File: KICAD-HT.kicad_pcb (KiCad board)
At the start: 2 copper layers, 90 x 70 mm, 86 parts, among them J1 HV80_IN, Q1 IPD050N10N5, Q2 IPD050N10N5, Q3 BSS127I, Q4 MMBT2222, Q5 BSS127I, T1 MSD1514-103ME, U1 UCC27517, U10 ISO7710, U11 AMC0311R, U12 UCC24612, U3 ISO7710, U5 DPC817, U7 AMC0311R, U8 AMC0311R, U9 AMC0302R

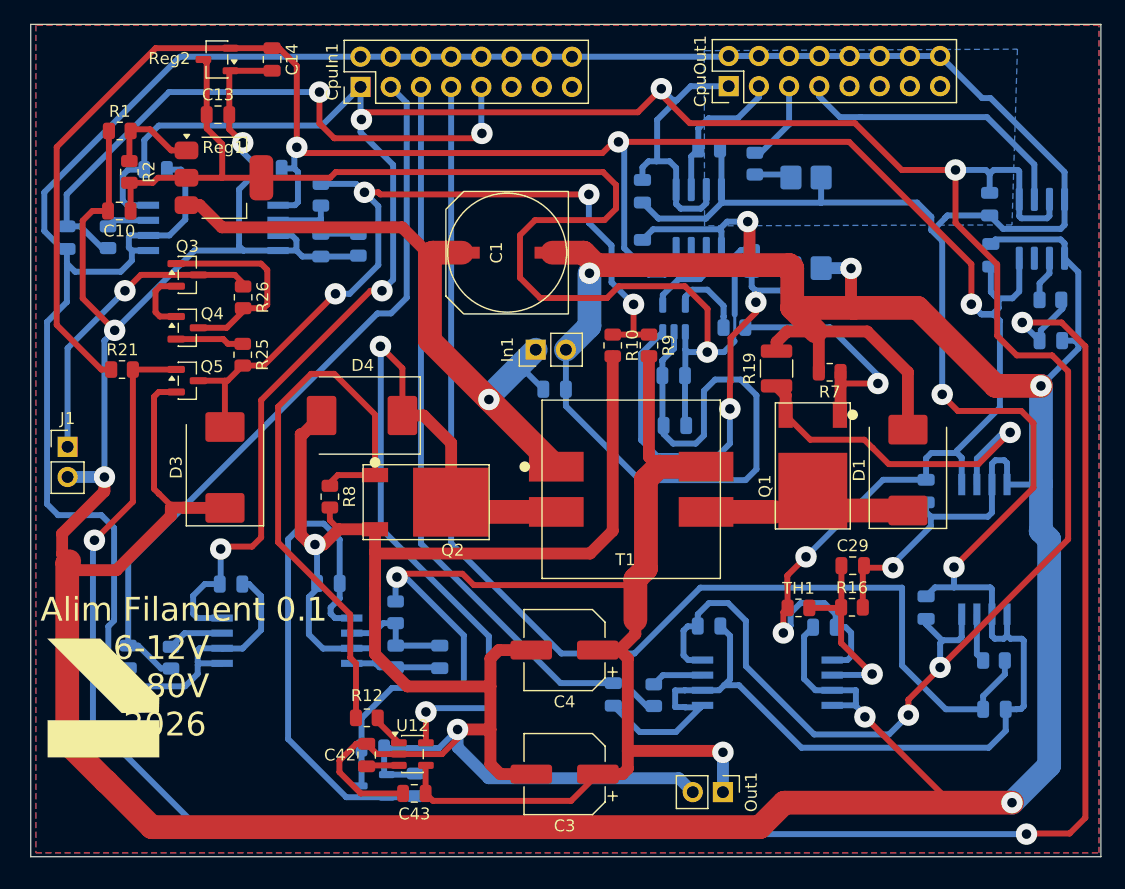
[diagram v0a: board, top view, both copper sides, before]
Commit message: Finalise le renommage alim-flyback-filament -> KICAD-HT et partage TO252
- Renommage du depot (fichiers deja renommes localement, jamais commite) :
  KICAD-HT.kicad_pcb/.kicad_pro/.kicad_sch, doc/KICAD-HT.png, references
  mises a jour (README.md, gen_composants.py PROJECT=, 00-intention-
  conception.md, doc/sim-vs-mesure.md, simulation/gen_asc.py).
  alim/isolation/polarisation.kicad_sch : resauvegarde native KiCad
  (reformatage), pas de changement electrique.
- bom_family_report.py : plus de chemin KiCad code en dur, detection
  dynamique du titre de projet (deja fait en session precedente, jamais
  commite).
- TO252 bascule vers la bibliotheque partagee lib_fp_commun/ (voir
  KICAD.md) : fp-lib-table pointe maintenant vers
  ${KIPRJMOD}/../lib_fp_commun/TO252.pretty au lieu de la copie locale,
  copie locale supprimee. Autres empreintes custom (A786, MSD1514,
  SOIC_DWV) : chemin de modele 3D repointe vers lib_fp_commun/ (les
  fichiers sources ont ete deplaces hors de composants-datasheets/datasheets/,
  qui ne garde plus que des PDF).

Co-Authored-By: Claude Sonnet 5 <noreply@anthropic.com>
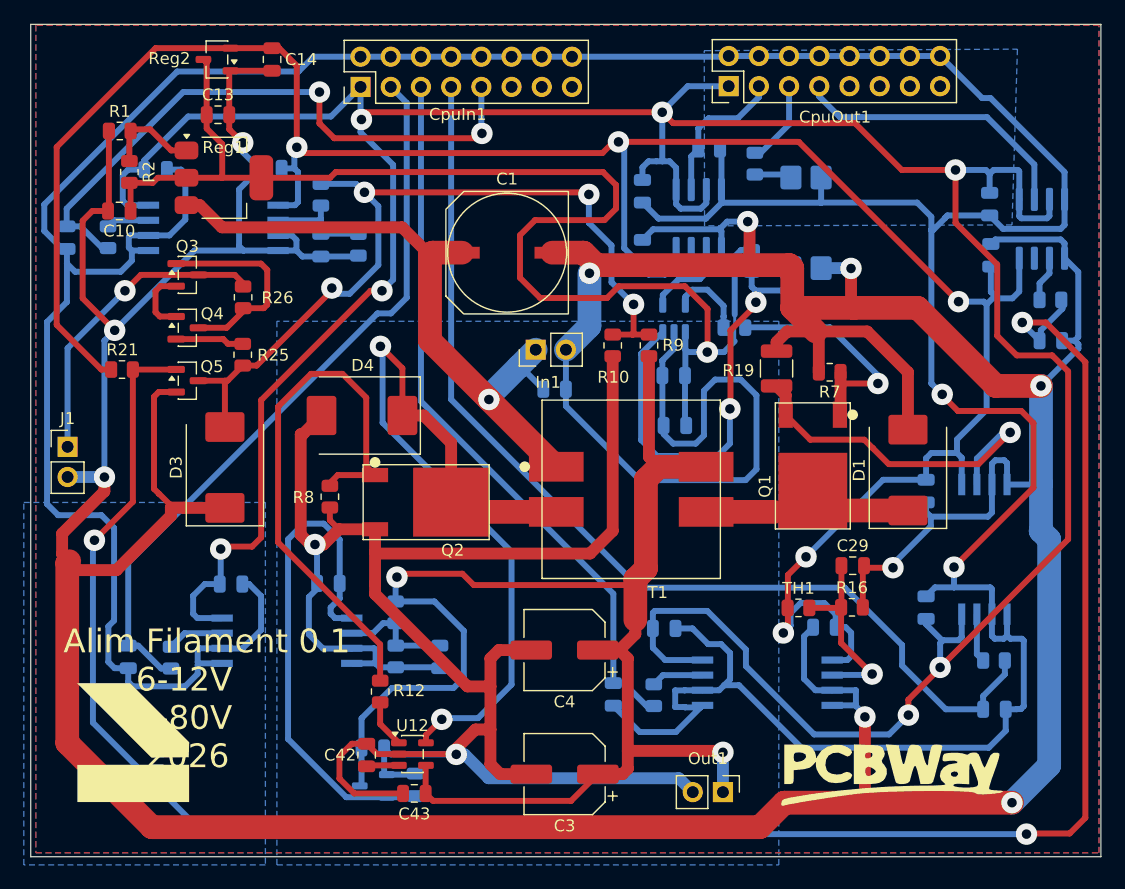
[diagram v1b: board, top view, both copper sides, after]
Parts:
- added G***: LOGO, lebel:pcbway-logo-small, F.Cu at (98.7, 83.6)
- moved ? 4.51 mm to (34.9, 81.2)
- moved C26 3.78 mm to (79.3, 71.6)
- moved R12 2.48 mm to (55.4, 76.9), turned to 90 degrees
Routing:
- net ISENSE_PRI_FBACK: track 102.2 -> 87.7 mm
- net RAIL_3V3_PRI: track 207.1 -> 202.5 mm
- net VOUT_N: track 172.2 -> 167.7 mm
- net GND: track 482.0 -> 486.3 mm
- net TEMP_PRI_FBACK: track 63.6 -> 61.0 mm
- net GND_CTRL: track 348.6 -> 350.8 mm
- net GATE_Q2: track 49.0 -> 47.1 mm
- net 3V3_CTRL: track 277.4 -> 275.8 mm
- net Net-(U12-VG): track 2.84 -> 4.05 mm
- net VOUT_P: track 125.3 -> 124.2 mm
- net SW_SEC: track 68.1 -> 69.0 mm
- net VAR_GATE: track 175.6 -> 174.8 mm
- net BIAS_FBACK: track 53.1 -> 52.4 mm
- net HV_BIAS: track 69.8 -> 70.3 mm
- added copper zone on B.Cu, net VOUT_N

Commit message: Bascule les empreintes custom (MSD1514, A786, SOIC_DWV) et logos (lebel/pcbway) vers lib_fp_commun
Supprime les copies locales redondantes, ajoute Symbol_commun/Graphic
(bibliotheques standard KiCad partagees) au fp-lib-table. Les logos
places sur le PCB passent du nickname lebel/lib au nickname partage
artwork (lib_id renomme directement sur les instances, pas de symbole
schema pour ces footprints decoratifs).

Co-Authored-By: Claude Sonnet 5 <noreply@anthropic.com>
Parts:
- removed ?: LOGO, lebel:lebel-logo
- removed CpuIn1: CTRL_C2000_IN, Connector_PinHeader_2.54mm:PinHeader_2x08_P2.54mm_Vertical
- removed CpuOut1: CTRL_C2000_OUT, Connector_PinHeader_2.54mm:PinHeader_2x08_P2.54mm_Vertical
- added G***: LOGO, artwork:lebel-logo-cartouche, F.Cu at (34.3, 82.3)
- added J2: NAPPE_FILAMENT_HT, Connector_IDC:IDC-Header_2x10_P2.54mm_Vertical, F.Cu at (127.4, 33.3)
- G***: footprint lebel:pcbway-logo-small -> artwork:pcbway-logo-small
- moved G*** 47.1 mm to (99.6, 36.6)
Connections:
- net 3V3_CTRL renamed 3V3_ISO
- net BIAS_FBACK renamed V_bias
- net ISENSE_PRI_FBACK renamed I_Shunt_ht
- net PWM_PRI_IN renamed PWM_ht
- net TEMP_PRI_FBACK renamed Temp_ht
- net VOUT_FBACK renamed Vht
- R3 pad 1: EN_PRI_IN -> PWM_EN
- U10 pad 2: PWM_BIAS_IN -> PWM_bias
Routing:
- net PWM_bias: track 0.00 -> 24.3 mm
- net PWM_BIAS_IN: track 24.3 -> 0.00 mm
- net PWM_EN: track 0.00 -> 7.10 mm
- net EN_PRI_IN: track 7.10 -> 0.00 mm

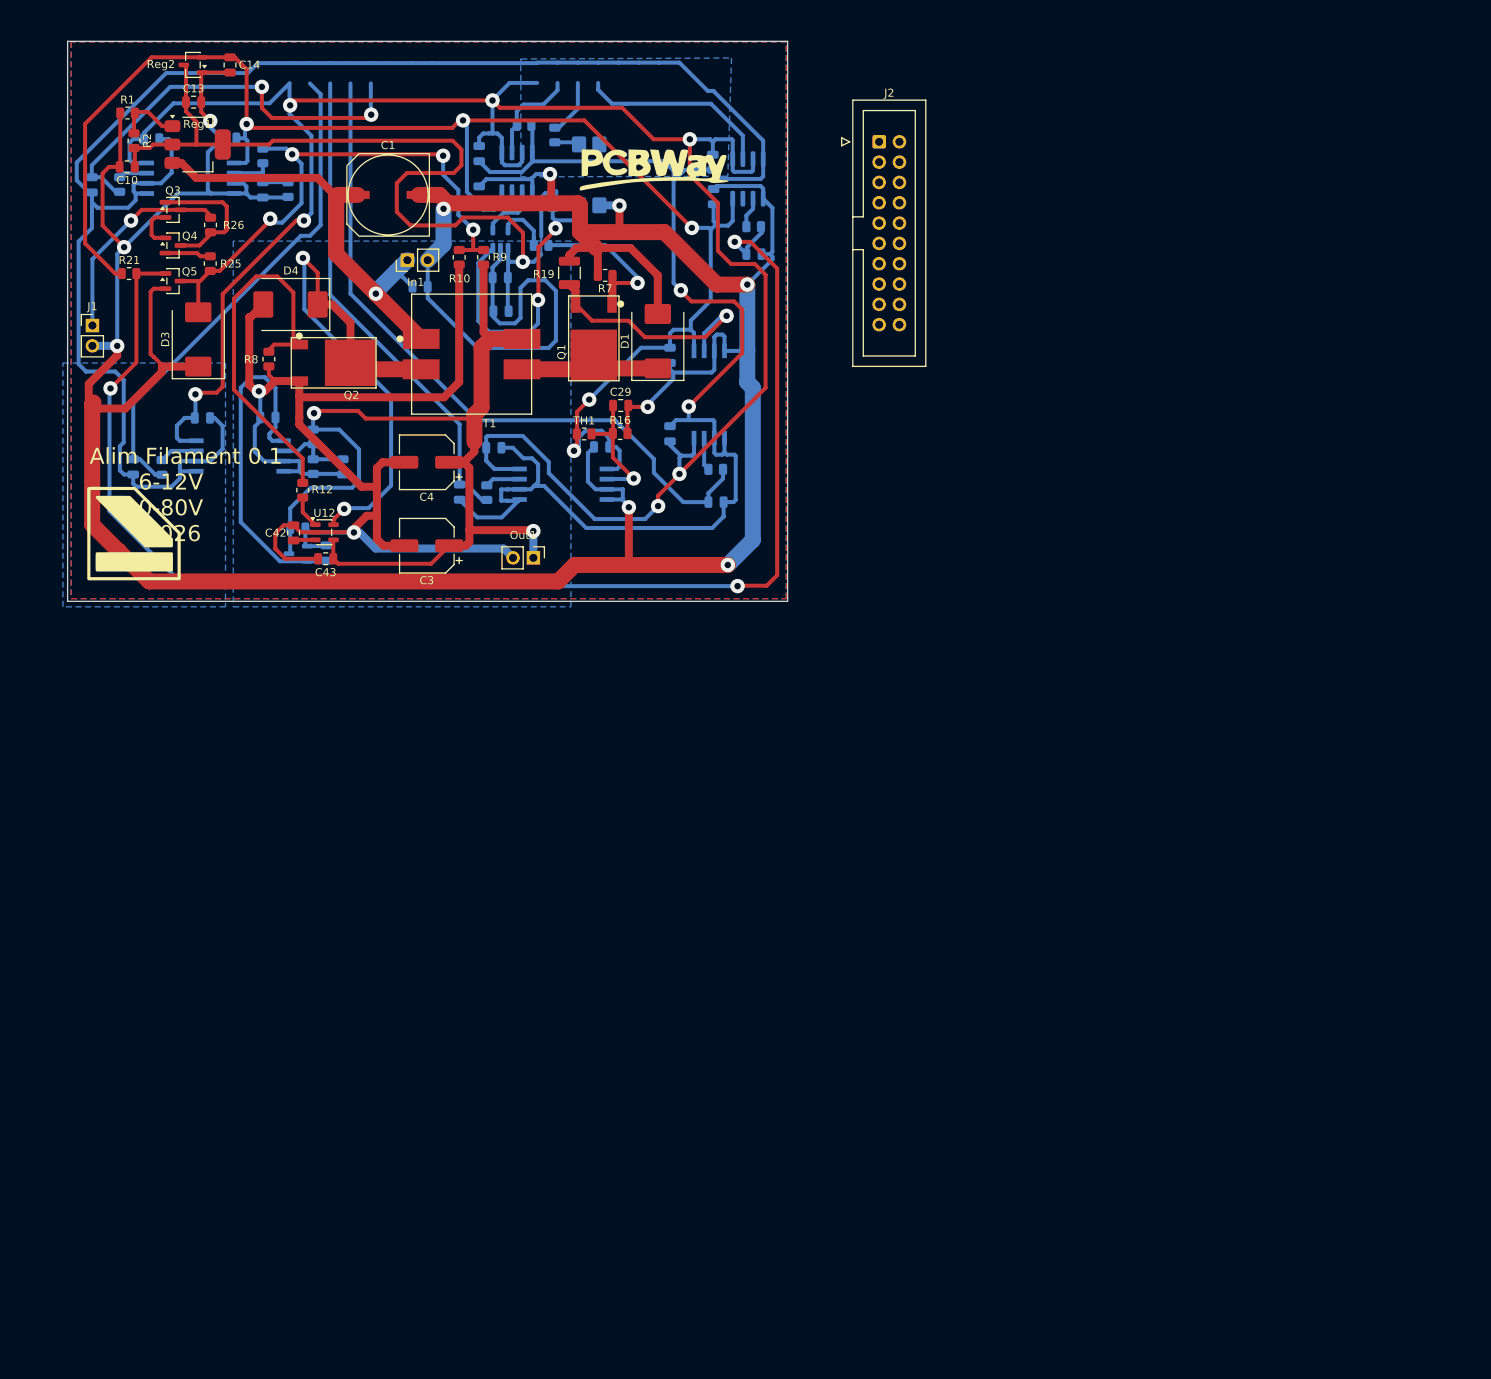
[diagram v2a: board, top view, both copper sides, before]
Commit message: Ajoute une LED de defaut sur Q_TRIP (R34/D6), corrige un bug d'insertion lib_symbols
Q_TRIP (sortie de reserve du verrou) recoit un usage reel : LED rouge 3mm
+ 10k, polarite ajustee par l'utilisateur pour s'allumer en defaut latche
(Q_TRIP -> D6 -> R34 -> GND, verifie par export netlist).

Corrige au passage une insertion incorrecte du bloc lib_symbols de
Device:LED (imbrique par erreur dans l'etiquette globale ISNS_AMP au lieu
de suivre la vraie fermeture de lib_symbols), qui empechait le chargement
de la feuille. Documente dans l'addendum du S19.

Co-Authored-By: Claude Sonnet 5 <noreply@anthropic.com>
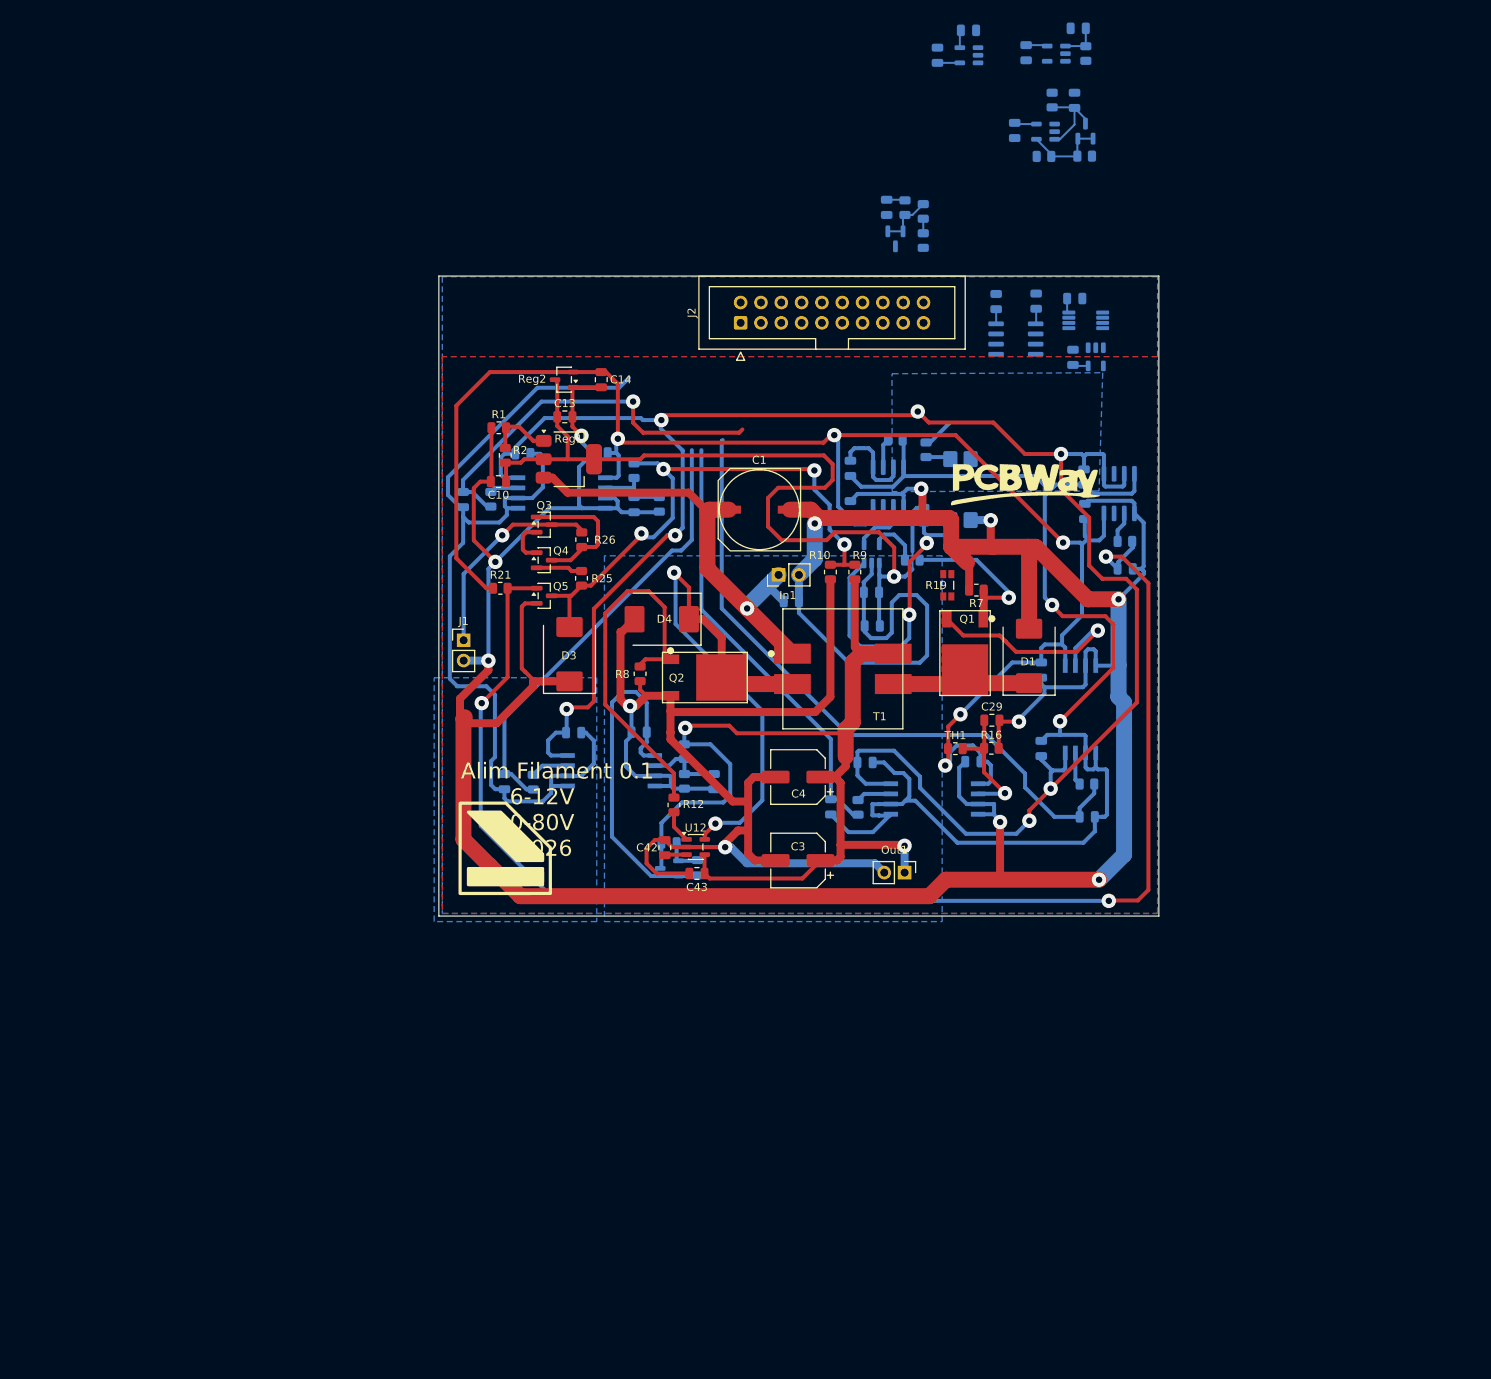
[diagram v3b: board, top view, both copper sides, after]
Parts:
- added C46: 100n, Capacitor_SMD:C_0805_2012Metric, B.Cu at (151.7, 60.2)
- added C47: 22p, Capacitor_SMD:C_0805_2012Metric, B.Cu at (151.8, 28.1)
- added C48: 100n, Capacitor_SMD:C_0805_2012Metric, B.Cu at (144.4, 31.9)
- added C50: 1n, Capacitor_SMD:C_0805_2012Metric, B.Cu at (134.7, 22.5)
- added C51: 100n, Capacitor_SMD:C_0805_2012Metric, B.Cu at (145.8, 22.2)
- added C52: 100p, Capacitor_SMD:C_0805_2012Metric, B.Cu at (152.3, 19.1)
- added C53: 100n, Capacitor_SMD:C_0805_2012Metric, B.Cu at (151.9, 52.9)
- added C54: 100n, Capacitor_SMD:C_0805_2012Metric, B.Cu at (138.6, 19.4)
- added C55: 100n, Capacitor_SMD:C_0805_2012Metric, B.Cu at (128.4, 41.5)
- added C56: 100n, Capacitor_SMD:C_0805_2012Metric, B.Cu at (142.1, 53.3)
- added C57: 100n, Capacitor_SMD:C_0805_2012Metric, B.Cu at (147.1, 53.2)
- added D5: BAT54S, Package_TO_SOT_SMD:SOT-23, B.Cu at (153.2, 32.0)
- added R27: 1k, Resistor_SMD:R_0805_2012Metric, B.Cu at (149.1, 28.1)
- added R28: 1.00k, Resistor_SMD:R_0805_2012Metric, B.Cu at (148.0, 35.1)
- added R29: 10k, Resistor_SMD:R_0805_2012Metric, B.Cu at (153.1, 35.1)
- added R30: 1k, Resistor_SMD:R_0805_2012Metric, B.Cu at (130.7, 41.5)
- added R31: 1k, Resistor_SMD:R_0805_2012Metric, B.Cu at (132.9, 42.0)
- added R32: 10k, Resistor_SMD:R_0805_2012Metric, B.Cu at (132.9, 45.7)
- added R33: 1k, Resistor_SMD:R_0805_2012Metric, B.Cu at (153.3, 22.3)
- added U13: SN74LVC1G08, Package_TO_SOT_SMD:SOT-23-5, B.Cu at (154.5, 60.2)
- added U14: TSV791, Package_TO_SOT_SMD:SOT-23-5, B.Cu at (148.2, 32.0)
- added U15: ATL431, Package_TO_SOT_SMD:SOT-23, B.Cu at (129.5, 45.4)
- added U16: LMV7219, Package_TO_SOT_SMD:SOT-23-5, B.Cu at (138.6, 22.5)
- added U17: SN74LVC1G132, Package_TO_SOT_SMD:SOT-23-5, B.Cu at (149.6, 22.3)
- added U18: SN74LVC1G74, Package_SO:VSSOP-8_3x3mm_P0.65mm, B.Cu at (153.2, 55.6)
- added U19: ISO7710F, Package_SO:SOIC-8_3.9x4.9mm_P1.27mm, B.Cu at (144.5, 58.0)
- C33: value 1n -> 47n
- R18: value 100 -> 1k
- R19: value 7m5 -> 10m; footprint Resistor_SMD:R_1210_3225Metric -> WSK1206:WSK1206R0100FEA
- moved R19 61.3 mm to (135.9, 88.7)
- moved C36 60.8 mm to (158.2, 86.7)
- moved Out1 60.8 mm to (130.6, 124.7)
- moved R18 60.8 mm to (153.4, 113.6)
- moved U8 60.8 mm to (134.3, 115.5)
- moved C1 60.8 mm to (112.5, 79.3)
- moved C10 60.8 mm to (79.8, 75.8)
- moved C14 60.8 mm to (92.7, 63.0)
- moved C15 60.8 mm to (123.8, 74.1)
- moved C16 60.8 mm to (123.8, 79.2)
- moved C18 60.8 mm to (97.4, 107.1)
- moved C19 60.8 mm to (126.5, 89.6)
- moved C21 60.8 mm to (126.6, 93.8)
- moved C23 60.8 mm to (106.8, 113.3)
- moved C24 60.8 mm to (80.6, 113.3)
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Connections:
- R19 pad 1: ISENSE_P -> ISNS_KP
- R19 pad 2: GND -> ISENSE_P
- U1 pad 3: EN_PRI_OUT -> EN_PRI_GATED
- U9 pad 2: ISENSE_P -> ISNS_KP
- U9 pad 3: GND -> ISNS_KN
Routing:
- net GND_CTRL: track 350.8 -> 281.3 mm
- net PWM_bias: track 24.3 -> 0.00 mm
- net RAIL_3V3_PRI: track 202.5 -> 220.6 mm
- net 3V3_ISO: track 275.8 -> 264.4 mm
- net ISNS_AMP_P: track 0.00 -> 11.1 mm
- net ISNS_AMP_FB: track 0.00 -> 10.3 mm
- net PWM_ht: track 12.5 -> 3.60 mm
- net GND: track 486.3 -> 478.1 mm
- net Vht: track 62.3 -> 55.3 mm
- net V_REF25: track 0.00 -> 6.89 mm
- net Temp_ht: track 61.0 -> 54.5 mm
- net I_Shunt_ht: track 87.7 -> 82.5 mm
- net PWM_LEB: track 0.00 -> 4.80 mm
- net V_TH: track 0.00 -> 4.61 mm
- net V_bias: track 52.4 -> 48.4 mm, vias 2 -> 1
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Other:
- board size 90 x 70 mm -> 90 x 80 mm
